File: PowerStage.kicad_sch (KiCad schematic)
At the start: 24 parts, among them U1 ECC81, U2 ECC82/12AU7, U3 ECC82/12AU7

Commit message: Initial schematic entry
Lets get started
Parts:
- added R16: 8, symbol Device:R
- added R17: 1M, symbol Device:R_US
- added V1: 260, symbol Simulation_SPICE:VDC
- added V2: 250, symbol Simulation_SPICE:VDC
- C1: renamed from C3; value ? nF -> 10n
- C2: renamed from C1; value ? nF -> 10n
- C3: renamed from C2; value ? nF -> 10n
- C4: renamed from C5; value C_Polarized_US -> 47u
- C5: renamed from C4; value 47µF -> 47u
- R1: renamed from R7; value R_US -> 10K
- R10: value R_US -> 1K
- R14: renamed from R13; value R_US -> 680
- R15: renamed from R12; value R_US -> 680
- R2: renamed from R5; value R_US -> 470K
- R3: renamed from R1; value 91K -> 68K
- R4: renamed from R3; value R_US -> 1.5K
- R5: renamed from R4; value R_US -> 22K
- R6: renamed from R2; value 100K -> 68K
- R7: renamed from R6; value R_US -> 470K
- R8: renamed from 470K1; value R_US -> 470K
- R9: renamed from 470K; value R_US -> 470K
- renumbered R8 to R12, R9 to R13, U2 to U1, U1 to U2
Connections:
- net B+OPT: now also V1.1
- net B+PI: now also V2.1
- net GND: now also C4.2, C5.2, R14.2, R15.2, R17.2, V1.2, V2.2
- net PI_Input: now also R17.1
- net at R15.1, U1.3 (K), U3.3 (K): now also C4.1
- net Fil1: now reaches U3.4 (F1)
- net Fil1: now also U1.4 (F1), U1.5 (F1), U2.4 (F1), U2.5 (F1), U3.5 (F1)
- net Fil2: now reaches U3.9 (F2)
- net Fil2: now also U1.9 (F2), U2.9 (F2)
- net at TR1.4 (Black): now also R16.1
- net at TR1.5 (Yellow): now also R16.2
- no-connect marks 0 -> 2
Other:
- moved on the sheet: C5, R12, R13, R14, R15, R9, U1A, U2C, U3A, U3C

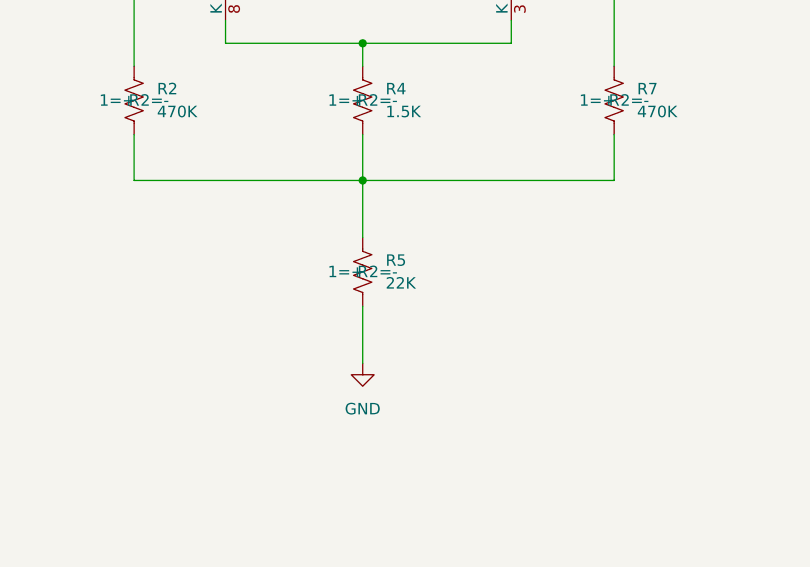
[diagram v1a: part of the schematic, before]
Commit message: .OP works
.OP works - Power stage initial DC operation ok.
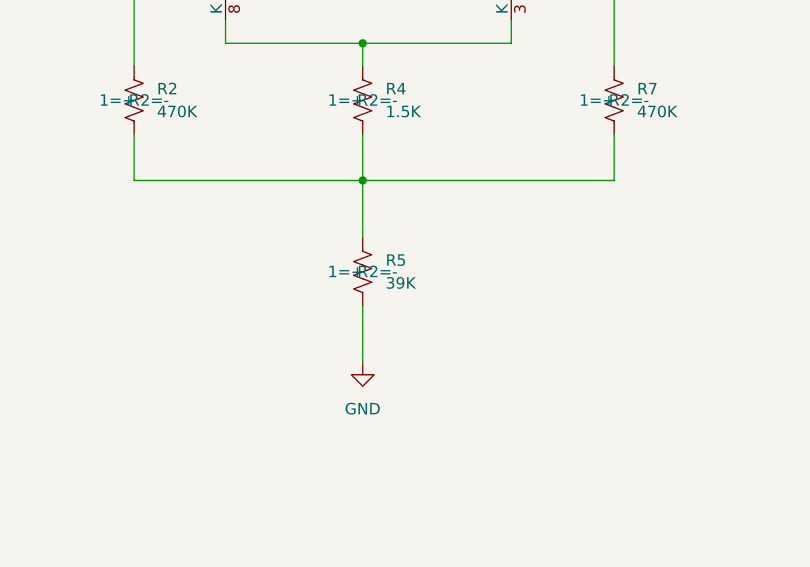
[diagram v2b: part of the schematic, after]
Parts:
- R5: value 22K -> 39K
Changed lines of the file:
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@@
 			)
 		)
-		(property "Sim.Library" "SPICE/Ayumi_LTspice/12AU7.inc"
+		(property "Sim.Library" "SPICE/Ayumi_LTspice/12AU7_DUAL.sub"
 			(at 190.5 104.14 0)
 			(hide yes)
@@
 			)
 		)
-		(property "Sim.Name" "12AU7"
+		(property "Sim.Name" "12AU7_DUAL"
 			(at 190.5 104.14 0)
 			(hide yes)
@@
 			)
 		)
-		(property "Sim.Pins" "1=A 2=G 3=K"
+		(property "Sim.Pins" "1=P1 2=G1 3=K1 6=P2 7=G2 8=K2"
 			(at 190.5 104.14 0)
 			(hide yes)
@@
 			)
 		)
-		(property "Value" "22K"
+		(property "Value" "39K"
 			(at 78.74 110.4899 0)
 			(show_name no)
@@
 			)
 		)
-		(property "Sim.Library" "SPICE/Ayumi_LTspice/12AU7.inc"
+		(property "Sim.Library" "SPICE/Ayumi_LTspice/12AU7_DUAL.sub"
 			(at 63.5 173.99 0)
 			(hide yes)
@@
 			)
 		)
-		(property "Sim.Name" "12AU7"
+		(property "Sim.Name" "12AU7_DUAL"
 			(at 63.5 173.99 0)
 			(hide yes)
@@
 			)
 		)
-		(property "Sim.Pins" "1=A 2=G 3=K"
+		(property "Sim.Pins" "1=P1 2=G1 3=K1 6=P2 7=G2 8=K2"
 			(at 63.5 173.99 0)
 			(hide yes)
@@
 			)
 		)
-		(property "Sim.Library" "SPICE/Ayumi_LTspice/12AU7.inc"
+		(property "Sim.Library" "SPICE/Ayumi_LTspice/12AU7_DUAL.sub"
 			(at 190.5 129.54 0)
 			(hide yes)
@@
 			)
 		)
-		(property "Sim.Name" "12AU7"
+		(property "Sim.Name" "12AU7_DUAL"
 			(at 190.5 129.54 0)
 			(hide yes)
@@
 			)
 		)
-		(property "Sim.Pins" "1=A 2=G 3=K"
+		(property "Sim.Pins" "1=P1 2=G1 3=K1 6=P2 7=G2 8=K2"
 			(at 190.5 129.54 0)
 			(hide yes)
@@
 			)
 		)
-		(property "Sim.Library" "SPICE/Ayumi_LTspice/12AU7.inc"
+		(property "Sim.Library" "SPICE/Ayumi_LTspice/12AU7_DUAL.sub"
 			(at 190.5 63.5 0)
 			(hide yes)
@@
 			)
 		)
-		(property "Sim.Name" "12AU7"
+		(property "Sim.Name" "12AU7_DUAL"
 			(at 190.5 63.5 0)
 			(hide yes)
@@
 			)
 		)
-		(property "Sim.Pins" "1=A 2=G 3=K"
+		(property "Sim.Pins" "1=P1 2=G1 3=K1 6=P2 7=G2 8=K2"
 			(at 190.5 63.5 0)
 			(hide yes)
@@
 			)
 		)
-		(property "Sim.Library" "SPICE/12AT7EH.i5.sub.txt"
+		(property "Sim.Library" "SPICE/12AT7_DUAL.sub"
 			(at 63.5 71.12 0)
 			(hide yes)
@@
 			)
 		)
-		(property "Sim.Name" "12AT7EH_i5"
+		(property "Sim.Name" "12AT7_DUAL"
 			(at 63.5 71.12 0)
 			(hide yes)
@@
 			)
 		)
-		(property "Sim.Pins" "1=A 2=G 3=K"
+		(property "Sim.Pins" "1=P1 2=G1 3=K1 6=P2 7=G2 8=K2"
 			(at 63.5 71.12 0)
 			(hide yes)
@@
 			)
 		)
-		(property "Sim.Library" "SPICE/Ayumi_LTspice/12AU7.inc"
+		(property "Sim.Library" "SPICE/Ayumi_LTspice/12AU7_DUAL.sub"
 			(at 190.5 40.64 0)
 			(hide yes)
@@
 			)
 		)
-		(property "Sim.Name" "12AU7"
+		(property "Sim.Name" "12AU7_DUAL"
 			(at 190.5 40.64 0)
 			(hide yes)
@@
 			)
 		)
-		(property "Sim.Pins" "1=A 2=G 3=K"
+		(property "Sim.Pins" "1=P1 2=G1 3=K1 6=P2 7=G2 8=K2"
 			(at 190.5 40.64 0)
 			(hide yes)
@@
 			)
 		)
-		(property "Sim.Library" "SPICE/Ayumi_LTspice/12AU7.inc"
+		(property "Sim.Library" "SPICE/Ayumi_LTspice/12AU7_DUAL.sub"
 			(at 36.83 173.99 0)
 			(hide yes)
@@
 			)
 		)
-		(property "Sim.Name" "12AU7"
+		(property "Sim.Name" "12AU7_DUAL"
 			(at 36.83 173.99 0)
 			(hide yes)
@@
 			)
 		)
-		(property "Sim.Pins" "1=A 2=G 3=K"
+		(property "Sim.Pins" "1=P1 2=G1 3=K1 6=P2 7=G2 8=K2"
 			(at 36.83 173.99 0)
 			(hide yes)
@@
 			)
 		)
-		(property "Sim.Library" "SPICE/12AT7EH.i5.sub.txt"
+		(property "Sim.Library" "SPICE/12AT7_DUAL.sub"
 			(at 88.9 173.99 0)
 			(hide yes)
@@
 			)
 		)
-		(property "Sim.Name" "12AT7EH_i5"
+		(property "Sim.Name" "12AT7_DUAL"
 			(at 88.9 173.99 0)
 			(hide yes)
@@
 			)
 		)
-		(property "Sim.Pins" "1=A 2=G 3=K"
+		(property "Sim.Pins" "1=P1 2=G1 3=K1 6=P2 7=G2 8=K2"
 			(at 88.9 173.99 0)
 			(hide yes)
@@
 			)
 		)
-		(property "Sim.Library" "SPICE/12AT7EH.i5.sub.txt"
+		(property "Sim.Library" "SPICE/12AT7_DUAL.sub"
 			(at 90.17 71.12 0)
 			(hide yes)
@@
 			)
 		)
-		(property "Sim.Name" "12AT7EH_i5"
+		(property "Sim.Name" "12AT7_DUAL"
 			(at 90.17 71.12 0)
 			(hide yes)
@@
 			)
 		)
-		(property "Sim.Pins" "1=A 2=G 3=K"
+		(property "Sim.Pins" "1=P1 2=G1 3=K1 6=P2 7=G2 8=K2"
 			(at 90.17 71.12 0)
 			(hide yes)

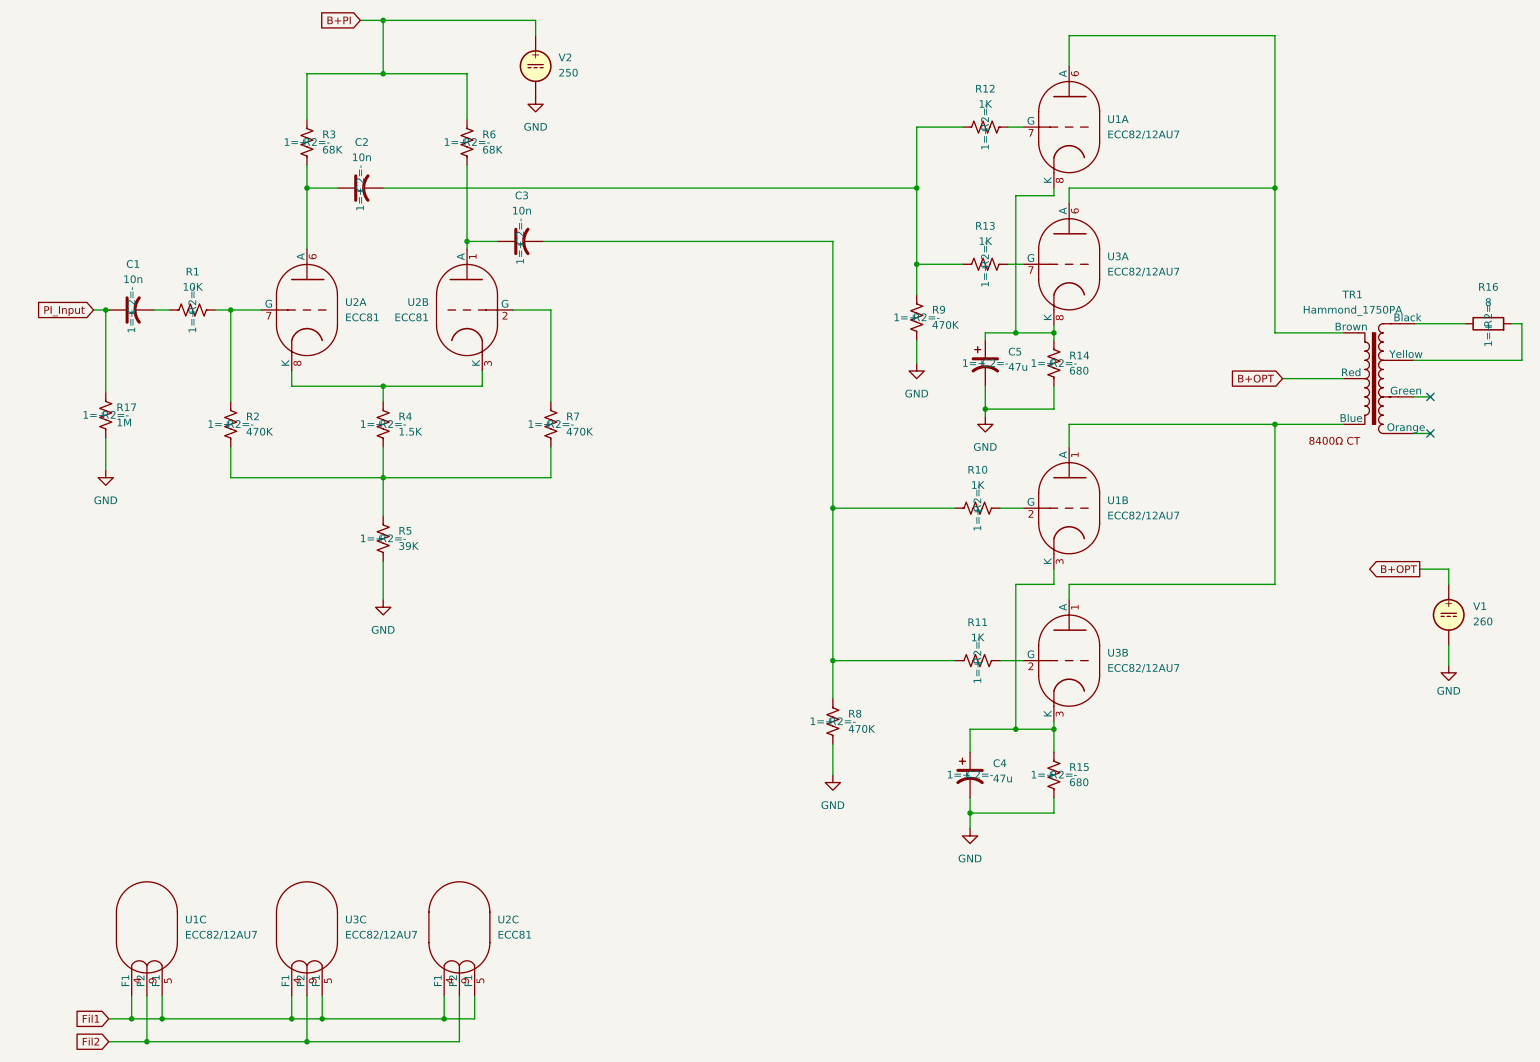
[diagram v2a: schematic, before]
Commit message: PI and output appear to work
First pass for output stage that looks ok in spice.
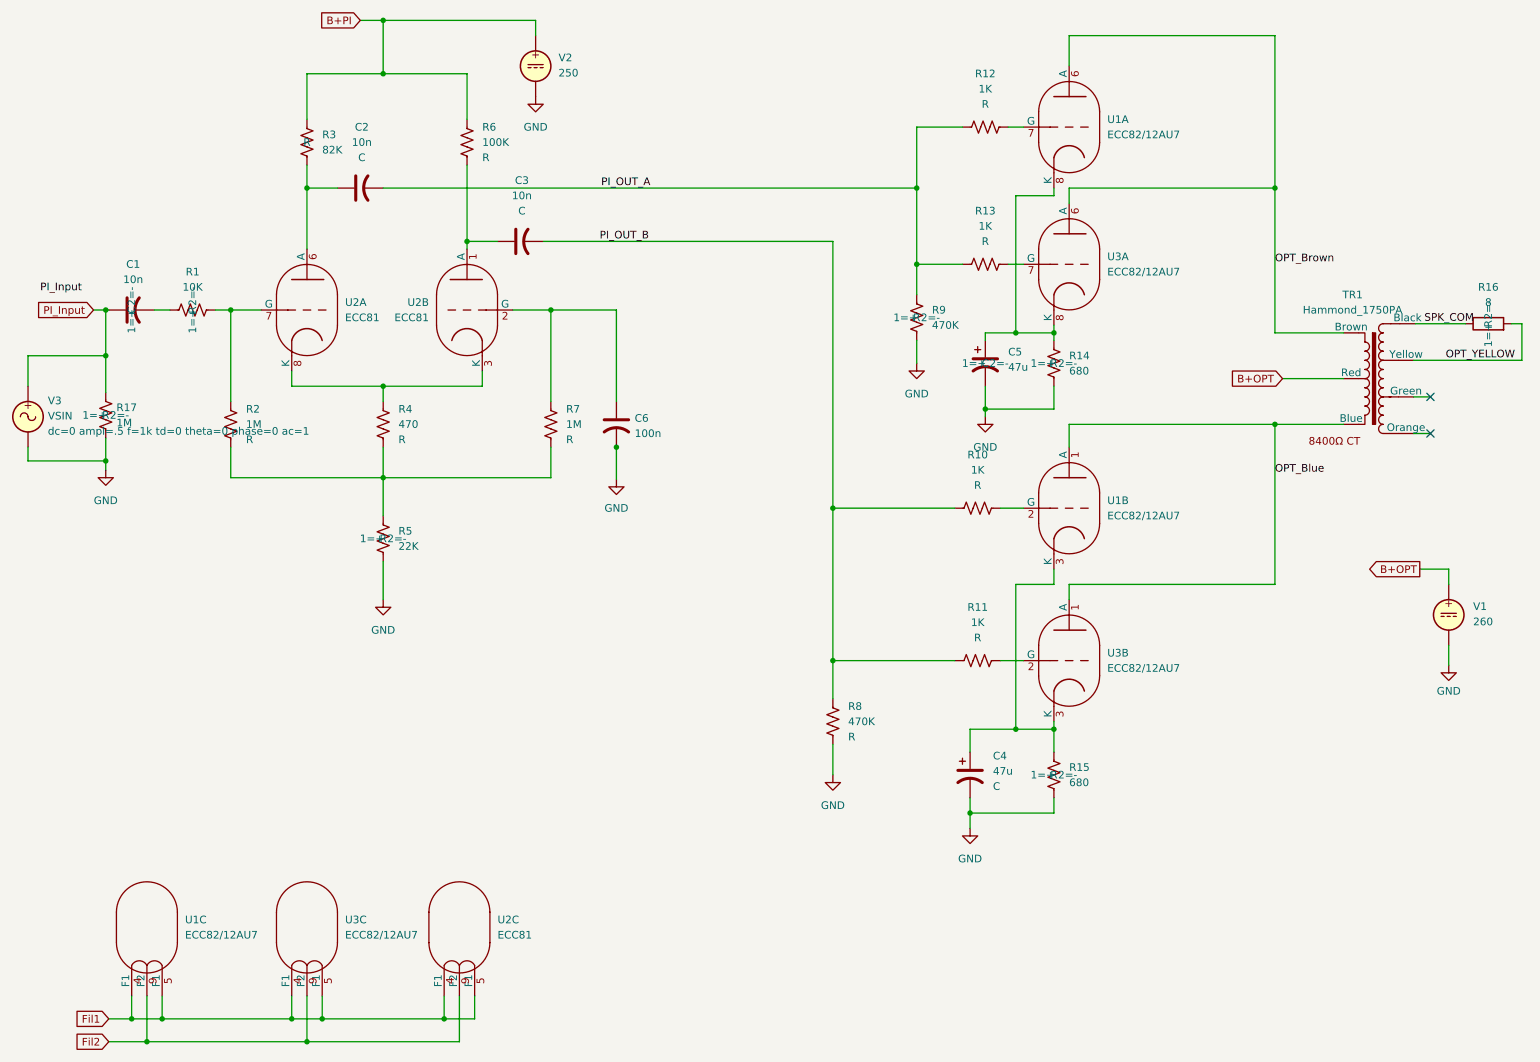
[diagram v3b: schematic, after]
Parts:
- added C6: 100n, symbol Device:C_US
- added V3: VSIN, symbol Simulation_SPICE:VSIN
- R2, R7: value 470K -> 1M
- R3: value 68K -> 82K
- R4: value 1.5K -> 470
- R5: value 39K -> 22K
- R6: value 68K -> 100K
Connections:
- net GND: now also C6.2, V3.2
- net PI_Input: now also V3.1
- net OPT_Blue: now reaches TR1.3 (Blue), U1.1 (A), U3.1 (A)
- net PI_OUT_A: now reaches C2.2, R12.1, R13.1, R9.1
- net OPT_Brown: now reaches TR1.1 (Brown), U1.6 (A), U3.6 (A)
- net SPK_COM: now reaches R16.1, TR1.4 (Black)
- net OPT_YELLOW: now reaches R16.2, TR1.5 (Yellow)
- net PI_OUT_B: now reaches C3.2, R10.1, R11.1, R8.1
- net at R7.2, U2.2 (G): now also C6.1

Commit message: Add Rectifier PCB
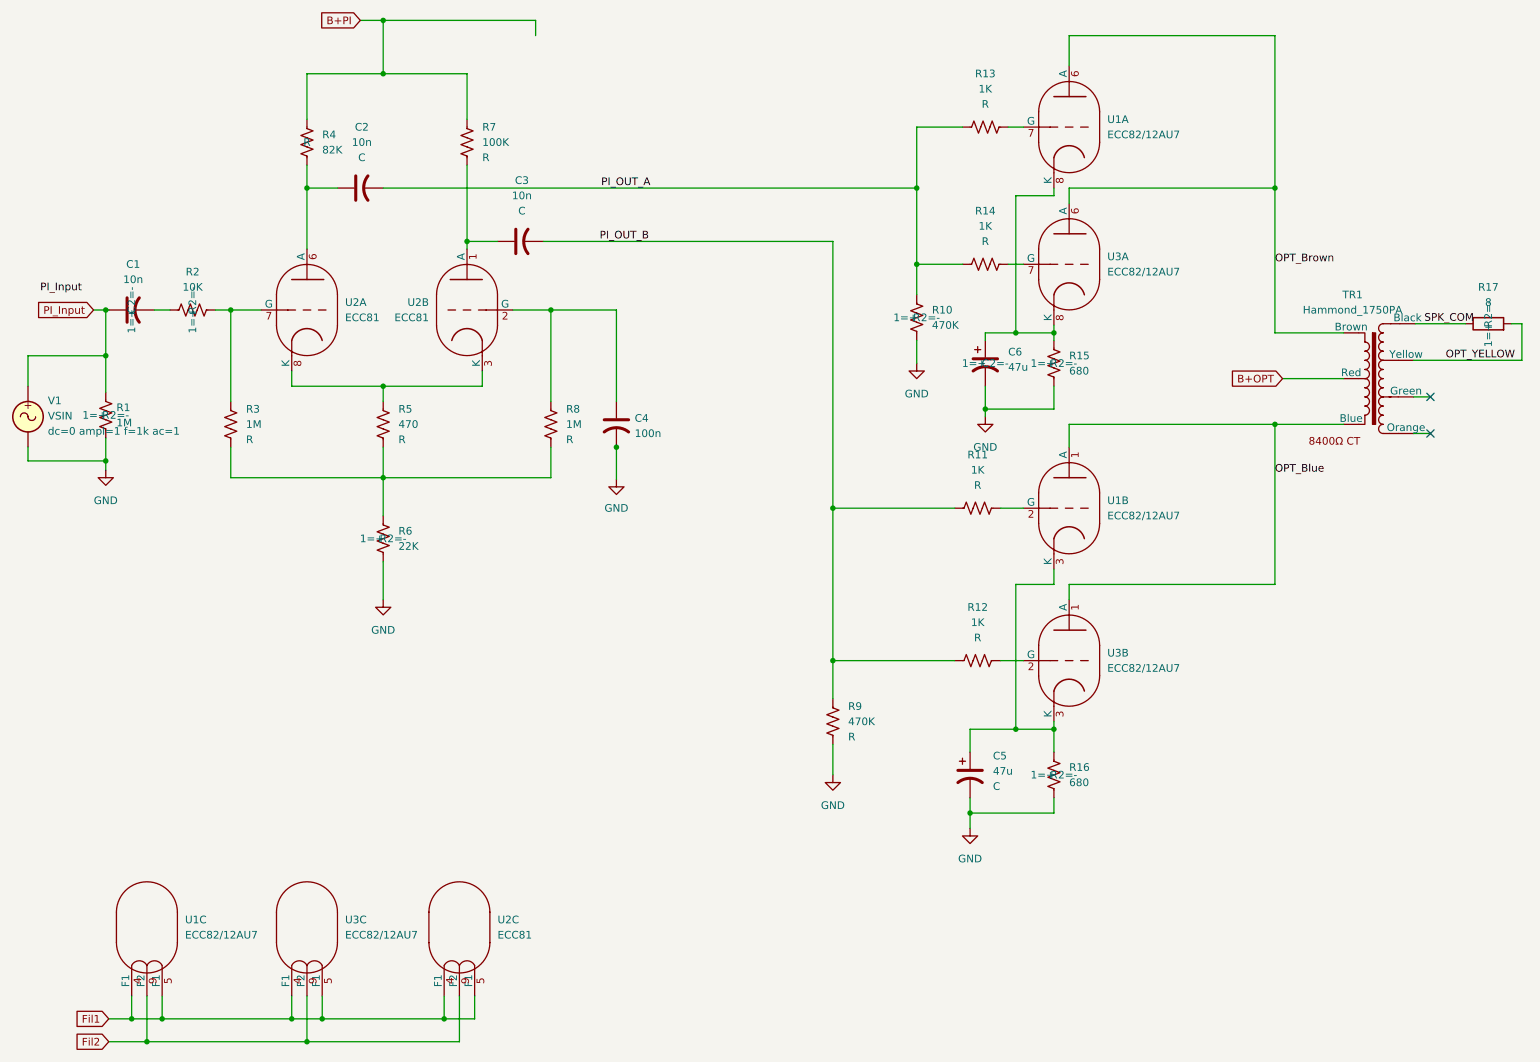
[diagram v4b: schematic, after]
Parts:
- removed V1: 260, symbol Simulation_SPICE:VDC
- removed V2: 250, symbol Simulation_SPICE:VDC
- renumbered C6 to C4, C4 to C5, C5 to C6, R17 to R1, R9 to R10, R10 to R11, R11 to R12, R12 to R13, R13 to R14, R14 to R15, R15 to R16, R16 to R17, R1 to R2, R2 to R3, R3 to R4, R4 to R5, R5 to R6, R6 to R7, R7 to R8, R8 to R9, V3 to V1
